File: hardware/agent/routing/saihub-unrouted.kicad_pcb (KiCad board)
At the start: 2 copper layers, 48 x 28 mm, 55 parts, among them J1 USB4105-GF-A, J2 1x12 2.54mm right-angle, Q1 AO3400A, SW1 BOOT, U1 USBLC6-2SC6, U2 SGM6232YPS8G/TR, U3 ESPC5-32E-H4, U4 TPS2553DBVR, U5 TPS2553DBVR

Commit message: feat(hardware): add header protection and refresh board deliverables
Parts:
- removed R13, R14: 10k, Saihub:R_0603_1608Metric
- added C21: 100n, Saihub:C_0603_1608Metric, F.Cu at (6.00, 4.30)
- added U10: USBLC6-2SC6, Saihub:SOT-23-6, F.Cu at (2.50, 5.50)
- added U6: TPD4E05U06DQAR, Saihub:TPD4E05U06_DQA, F.Cu at (14.5, 4.30)
- added U7: TPD4E05U06DQAR, Saihub:TPD4E05U06_DQA, F.Cu at (22.2, 4.30)
- D3: value SS14 -> SS34
- R10, R12, R9: value 100k -> 10k
- U4, U5: value TPS2553DBVR -> TPS2553DDBVR
- moved Q1 18.0 mm to (2.50, 25.5)
- moved R6 11.2 mm to (2.50, 15.8)
- moved C6 3.30 mm to (2.50, 8.80), turned to 0 degrees
- moved R11 2.36 mm to (15.3, 27.0)
- moved R12 2.05 mm to (22.0, 27.0), turned to 0 degrees
- moved U3 1.95 mm to (14.5, 15.6)
- moved TP3 1.90 mm to (5.60, 27.0)
- moved TP4 1.90 mm to (7.80, 27.0)
- moved TP5 1.90 mm to (10.0, 27.0)
- moved TP6 1.90 mm to (12.2, 27.0)
- moved C13 1.80 mm to (18.5, 27.0)
- moved C8 1.70 mm to (2.50, 14.1), turned to 0 degrees
- moved C7 1.70 mm to (2.50, 10.7), turned to 0 degrees
- moved TP1 0.80 mm to (1.20, 22.3)
- moved TP2 0.80 mm to (3.40, 22.3)
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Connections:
- U3 pad 19: (no net) -> FAULT4
- U3 pad 5: (no net) -> FAULT5

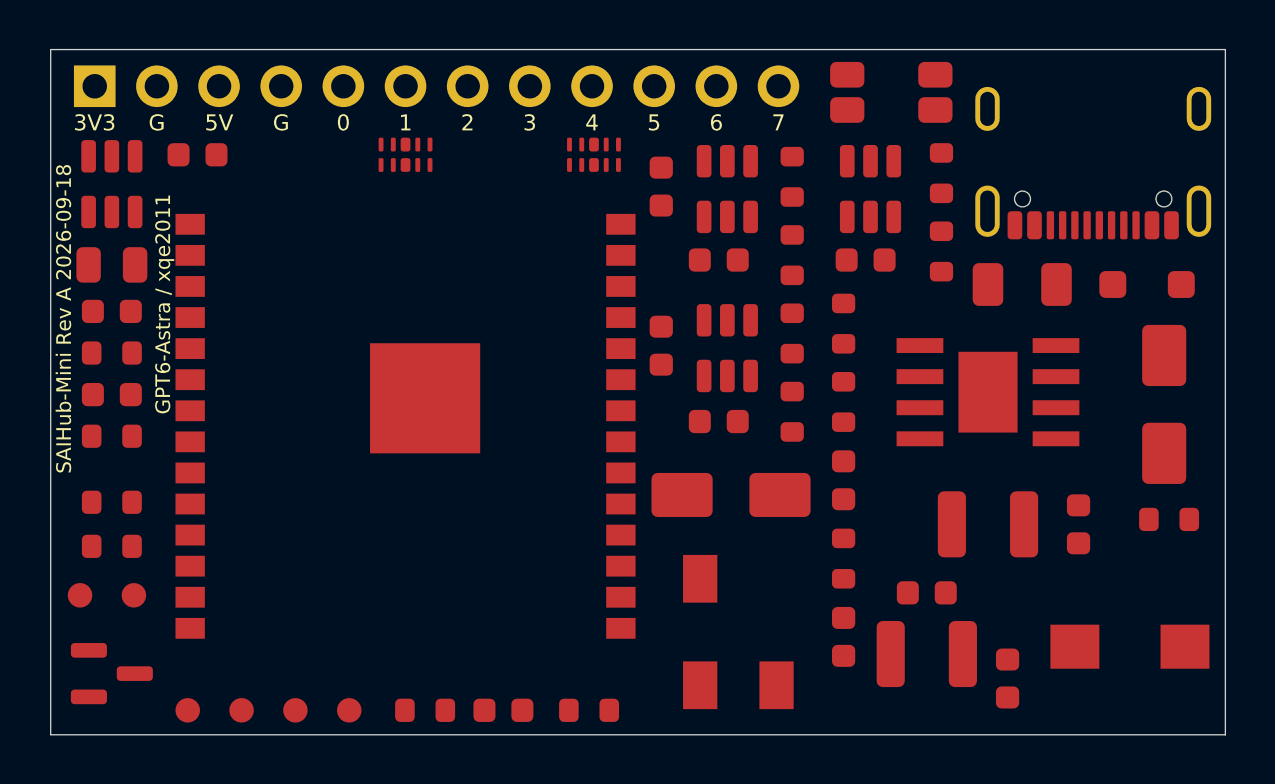
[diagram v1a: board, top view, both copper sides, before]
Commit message: Replace button and add corner antenna module without enlarging PCB
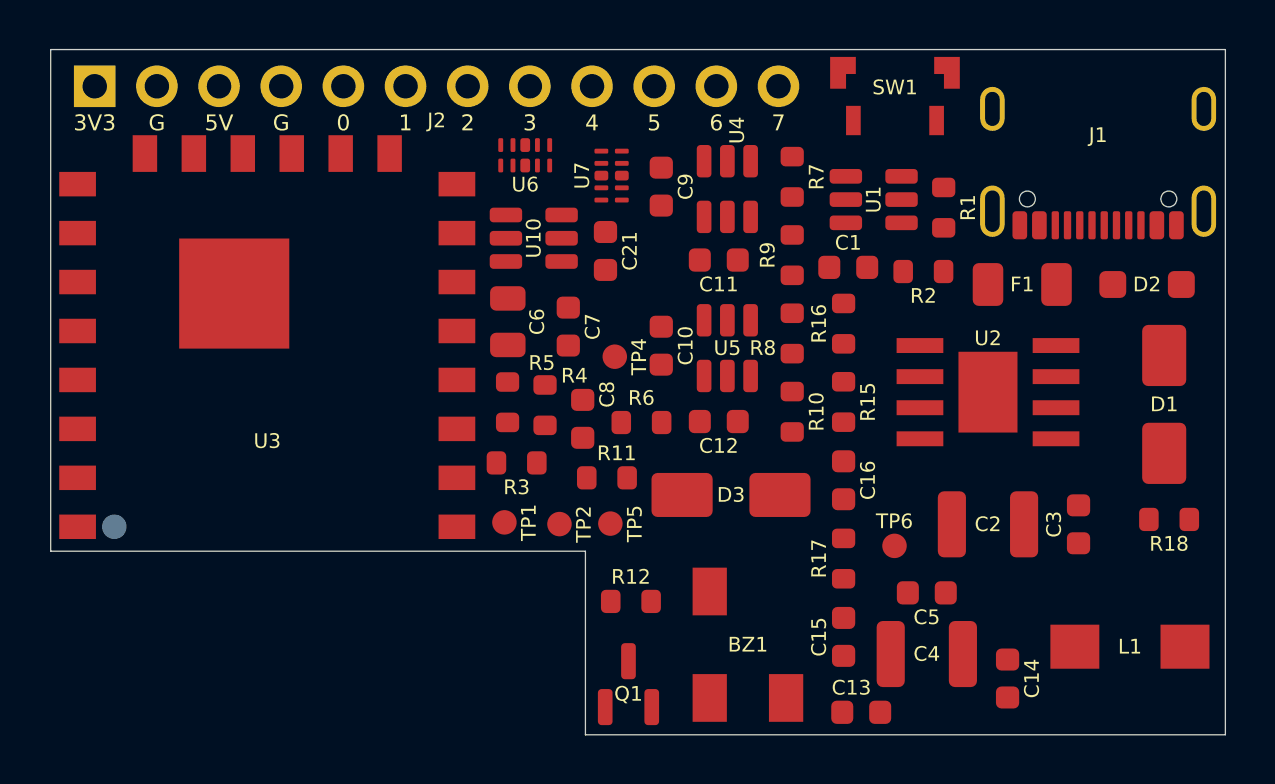
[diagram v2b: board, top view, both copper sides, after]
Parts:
- SW1: footprint Saihub:SW_SPST_EVQP7A -> Saihub:SW_SPST_TS2435VS
- TP3: moved to B.Cu
- U3: value ESPC5-32E-H4 -> ESPC5-12-H4; footprint Saihub:ESPC5-32E-H4 -> Saihub:ESPC5-12-H4
- moved TP6 23.3 mm to (34.5, 20.3)
- moved R6 21.6 mm to (24.1, 15.2), turned to 180 degrees
- moved Q1 21.1 mm to (23.6, 25.9), turned to 90 degrees
- moved TP4 21.0 mm to (23.1, 12.6)
- moved C8 19.3 mm to (21.7, 15.1), turned to 90 degrees
- moved C7 18.7 mm to (21.1, 11.3), turned to 90 degrees
- moved R4 18.6 mm to (20.2, 14.5), turned to 90 degrees
- moved TP2 17.6 mm to (20.8, 19.4)
- moved TP1 17.6 mm to (18.5, 19.3)
- moved U10 17.4 mm to (19.7, 7.71), turned to 180 degrees
- moved C21 17.1 mm to (22.7, 8.23), turned to 90 degrees
- moved R3 16.6 mm to (19.0, 16.9), turned to 180 degrees
- moved C6 16.3 mm to (18.7, 11.1), turned to 90 degrees
- moved R5 16.3 mm to (18.7, 14.4), turned to 90 degrees
- moved TP5 15.0 mm to (22.9, 19.4)
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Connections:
- U3 pad 1: GND -> IO2
- U3 pad 15: BOOT -> GND
- U3 pad 16: IO5 -> IO6
- U3 pad 17: IO4 -> FAULT4
- U3 pad 18: (no net) -> BOOT
- U3 pad 19: FAULT4 -> (no net)
- U3 pad 2: V3V3 -> IO1
- U3 pad 21: IO3 -> BUZZ_PWM
- U3 pad 22: (no net) -> UART_TX
- U3 pad 23: IO7 -> GND
- U3 pad 4: (no net) -> IO3
- U3 pad 6: IO2 -> IO4
- U3 pad 7: IO1 -> IO5
- U3 pad 8: IO6 -> V3V3
- U3 pad 9: (no net) -> IO7
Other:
- outline, holes or cut-outs redrawn
- board text added: "SAIHub-Mini Rev A 2026-09-24"
- board text removed: "SAIHub-Mini Rev A 2026-09-18"

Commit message: feat(hardware): add grouped indicators and reproducible routing
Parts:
- added D4: GREEN, Saihub:LED_AA1608, F.Cu at (30.3, 5.20)
- added D5: GREEN, Saihub:LED_AA1608, F.Cu at (30.3, 8.40)
- added D6: RED, Saihub:LED_AA1608, F.Cu at (30.3, 11.6)
- added D7: BLUE, Saihub:LED_AA1608, F.Cu at (30.3, 14.8)
- added R19: 680, Saihub:R_0603_1608Metric, B.Cu at (32.1, 5.20)
- added R20: 1.5k, Saihub:R_0603_1608Metric, B.Cu at (29.2, 8.05)
- added R21: 1.5k, Saihub:R_0603_1608Metric, B.Cu at (32.0, 10.8)
- added R22: 330, Saihub:R_0603_1608Metric, B.Cu at (30.4, 16.6)
- R10, R7, R8, R9: moved to B.Cu
- moved R8 4.31 mm to (26.0, 11.2), turned to 0 degrees
- moved R10 4.00 mm to (34.2, 14.2)
- moved R9 3.96 mm to (34.1, 9.50)
- moved R7 2.47 mm to (28.0, 4.30)
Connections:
- U3 pad 20: (no net) -> STATUS_LED

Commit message: fix(hardware): correct assembly footprints and package outlines
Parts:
- BZ1: value KLJ-5020 3.3V -> 5020 3V 4kHz; footprint Saihub:KLJ-5020 -> Saihub:Buzzer_5020_Supplied
- D4, D5, D6, D7: footprint Saihub:LED_AA1608 -> Saihub:LED_0603_1608Metric
- R19: value 680 -> 330
- R20: value 1.5k -> 1.2k
- SW1: footprint Saihub:SW_SPST_TS2435VS -> Saihub:SW_SPST_2X4_LocatingPins
- moved BZ1 0.50 mm to (28.5, 24.8), turned to 0 degrees
- turned D4 to -90 degrees
- turned D5 to -90 degrees
- turned D6 to -90 degrees
- turned D7 to 90 degrees
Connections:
- D4 pad 1: GND -> D4_A
- D4 pad 2: D4_A -> GND
- D5 pad 1: GND -> D5_A
- D5 pad 2: D5_A -> GND
- D6 pad 1: GND -> D6_A
- D6 pad 2: D6_A -> GND
- D7 pad 1: GND -> D7_A
- D7 pad 2: D7_A -> GND

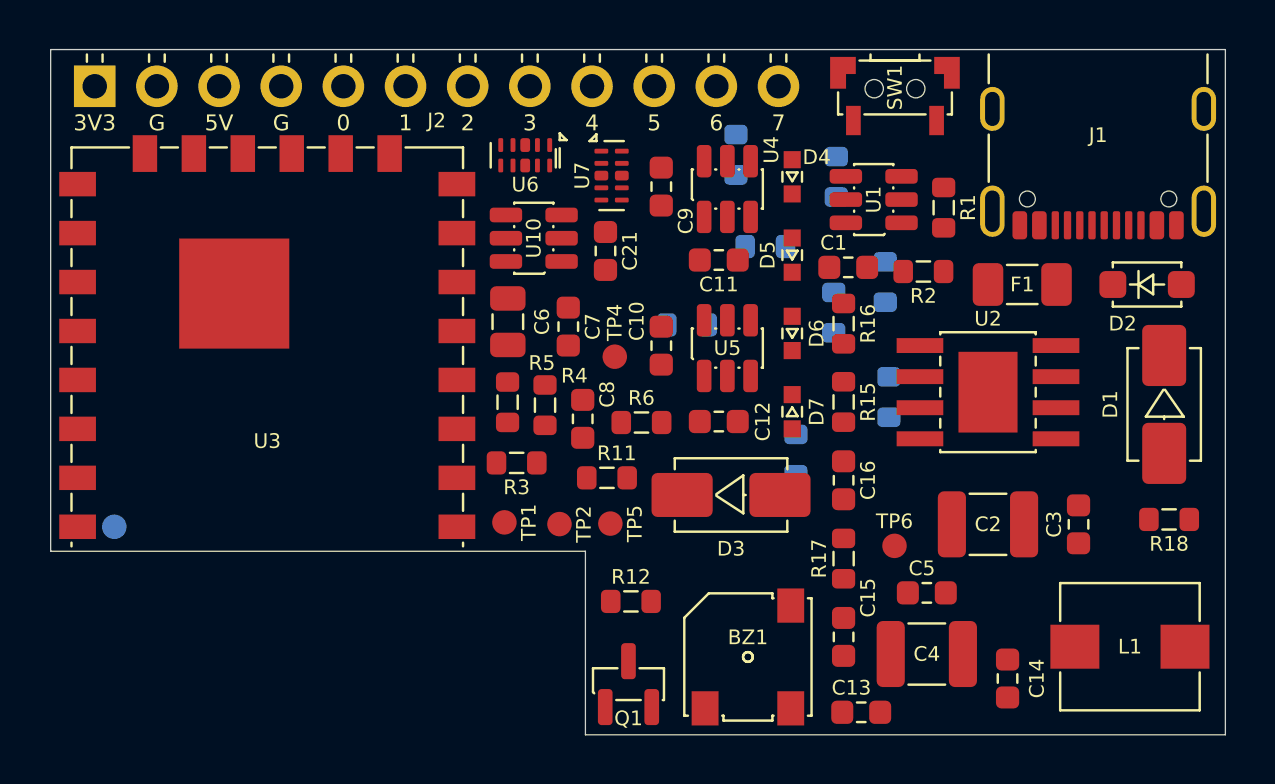
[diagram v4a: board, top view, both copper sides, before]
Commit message: fix(hardware): finish front-only PCB routing and review exports
Place all components and test pads on the front surface while preserving
the shell-critical connector, button, module and indicator positions.
Consolidate the four indicator resistors to 660 ohms, use the smaller
shared protection array at U10, and relocate support parts for local routing.

Complete all signal and ground connections, preserve the supply paths,
and capture replayable copper with the actual pour settings. Refresh the
schematic, interactive BOM, PCB and enclosure review documents.

Validation: zero ERC, DRC, schematic-parity and unconnected findings;
routing reconstruction passes; all six PDF pages visually reviewed.
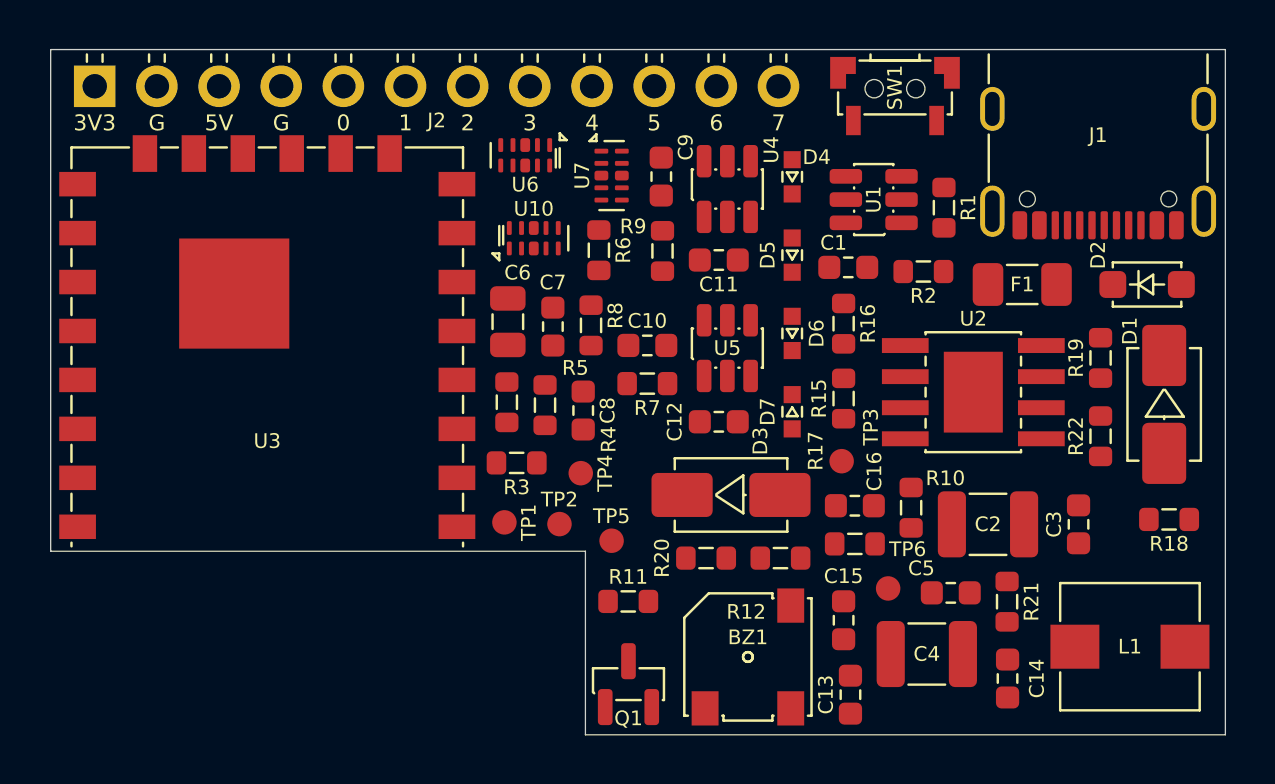
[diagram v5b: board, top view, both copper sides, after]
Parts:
- removed C21: 100n, Saihub:C_0603_1608Metric
- R10, R7, R8, R9, TP3: moved to F.Cu
- R19, R22: value 330 -> 660; moved to F.Cu
- R20: value 1.2k -> 660; moved to F.Cu
- R21: value 1.5k -> 660; moved to F.Cu
- U10: value USBLC6-2SC6 -> TPD4E05U06DQAR; footprint Saihub:SOT-23-6 -> Saihub:TPD4E05U06_DQA
- moved TP3 29.8 mm to (32.3, 16.8)
- moved R21 13.8 mm to (39.1, 22.6)
- moved R19 13.1 mm to (42.9, 12.6)
- moved R20 13.0 mm to (26.8, 20.8)
- moved R22 12.5 mm to (42.9, 15.8)
- moved R7 10.0 mm to (24.4, 13.7), turned to 0 degrees
- moved R9 9.19 mm to (25.0, 8.23)
- moved R6 7.25 mm to (22.4, 8.20), turned to -90 degrees
- moved R12 6.36 mm to (29.8, 20.8), turned to 0 degrees
- moved R11 5.12 mm to (23.6, 22.6), turned to 0 degrees
- moved TP4 4.96 mm to (21.7, 17.3)
- moved R10 4.61 mm to (35.2, 18.7)
- moved R8 3.92 mm to (22.1, 11.3), turned to 90 degrees
- moved TP6 1.76 mm to (34.2, 22.0)
- moved C16 1.14 mm to (32.9, 18.6), turned to 0 degrees
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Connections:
- J1 pad A8: (no net) -> unconnected-(J1-SBU1-PadA8)
- J1 pad B8: (no net) -> unconnected-(J1-SBU2-PadB8)
- U10 pad 2: GND -> unconnected-(U10-IO2-Pad2)
- U10 pad 3: V5_SW -> GND
- U10 pad 4: V5_SW -> unconnected-(U10-IO3-Pad4)
- U10 pad 5: V5 -> V5_SW
- U10 pad 6: V3_SW -> unconnected-(U10-NC-Pad6)
- U2 pad 7: (no net) -> unconnected-(U2-EN-Pad7)
- U3 pad 19: (no net) -> unconnected-(U3-GPIO27-Pad19)
- U6 pad 10: (no net) -> unconnected-(U6-NC-Pad10)
- U6 pad 6: (no net) -> unconnected-(U6-NC-Pad6)
- U6 pad 7: (no net) -> unconnected-(U6-NC-Pad7)
- U6 pad 9: (no net) -> unconnected-(U6-NC-Pad9)
- U7 pad 10: (no net) -> unconnected-(U7-NC-Pad10)
- U7 pad 6: (no net) -> unconnected-(U7-NC-Pad6)
- U7 pad 7: (no net) -> unconnected-(U7-NC-Pad7)
- U7 pad 9: (no net) -> unconnected-(U7-NC-Pad9)
